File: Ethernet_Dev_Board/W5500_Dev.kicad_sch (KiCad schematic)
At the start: 35 parts, among them Q201 PMV48XPA2R, U201 WIZNET_W5500, U202 74AUP1T08GWH, Y201 25MHz

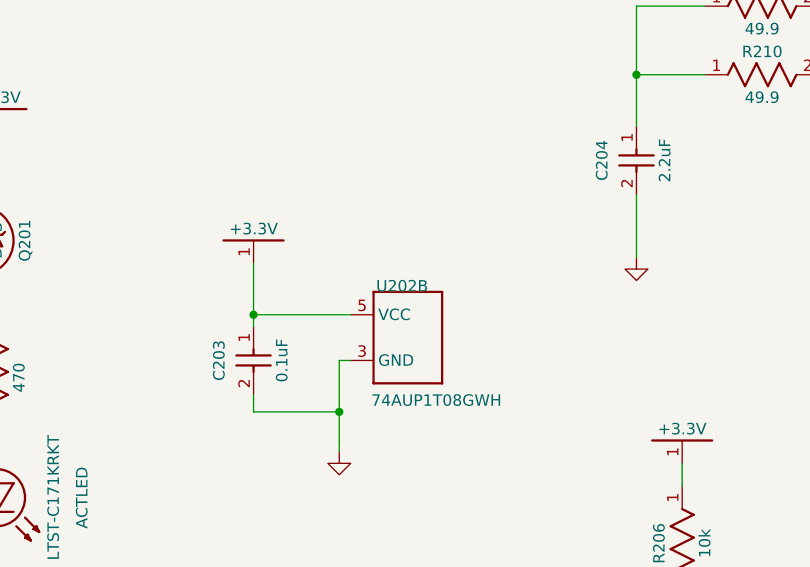
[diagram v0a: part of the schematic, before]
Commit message: Associating footprint to component
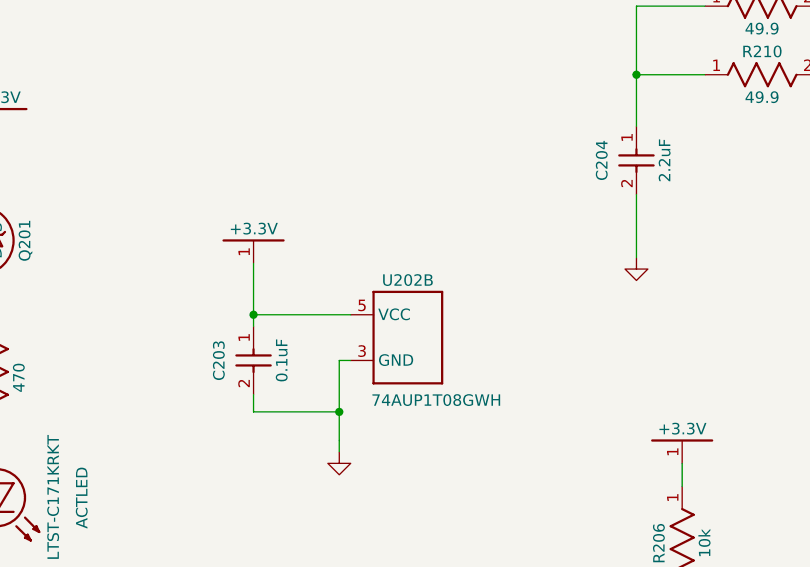
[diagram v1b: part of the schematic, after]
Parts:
- Y201: footprint (none) -> RG_Crystal:Crystal_SMD_4Pin_7.0mmx5.0mm
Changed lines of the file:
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@@
 			)
 		)
-		(property "Footprint" ""
+		(property "Footprint" "RG_Crystal:Crystal_SMD_4Pin_7.0mmx5.0mm"
 			(at 179.07 154.94 0)
 			(effects
@@
 		(dnp no)
 		(property "Reference" "U202"
-			(at 139.065 108.585 0)
-			(effects
-				(font
+			(at 139.7 107.95 0)
+			(effects
+				(font

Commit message: Net adjustments. Beginning board layout
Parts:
- LED201: value ACTLED -> 5500 ACT
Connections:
- net GNDS: no longer C201.2, C202.2, C203.2, C204.2, C205.2, C206.2, C209.2, C210.2, R201.2, R202.10 (1@2), R204.1, U201.14 (AGND@1), U201.16 (AGND@2), U201.19 (AGND@3), U201.29 (GND), U201.3 (AGND@1), U201.48 (AGND), U201.9 (AGND@2), U202.3 (GND), Y201.2 (GND)
- net RXN renamed RX_N
- net RXN_ETH renamed ETH_RX_N
- net RXP renamed RX_P
- net RXP_ETH renamed ETH_RX_P
- net TXN renamed TX_N
- net TXN_ETH renamed ETH_TX_N
- net TXP renamed TX_P
- net TXP_ETH renamed ETH_TX_P
- new net GND1: C201.2, C202.2, C203.2, C204.2, C205.2, C206.2, C209.2, C210.2, R201.2, R202.10 (1@2), R204.1, U201.14 (AGND@1), U201.16 (AGND@2), U201.19 (AGND@3), U201.29 (GND), U201.3 (AGND@1), U201.48 (AGND), U201.9 (AGND@2), U202.3 (GND), Y201.2 (GND)
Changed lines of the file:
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@@
 	(wire
 		(pts
-			(xy 53.975 65.405) (xy 53.975 86.995)
-		)
-		(stroke
-			(width 0.25)
-			(type solid)
-		)
-	)
-	(wire
-		(pts
 			(xy 125.095 196.85) (xy 41.275 196.85)
 		)
@@
 		)
 		(stroke
-			(width 0.25)
-			(type solid)
+			(width 0)
+			(type default)
 		)
 	)
@@
 		)
 		(stroke
-			(width 0.25)
-			(type solid)
+			(width 0)
+			(type default)
 		)
 	)
@@
 		)
 		(stroke
-			(width 0.25)
-			(type solid)
+			(width 0)
+			(type default)
 		)
 	)
@@
 		)
 		(stroke
-			(width 0.25)
-			(type solid)
+			(width 0)
+			(type default)
 		)
 	)
@@
 		)
 		(stroke
-			(width 0.25)
-			(type solid)
+			(width 0)
+			(type default)
 		)
 	)
@@
 		)
 		(stroke
-			(width 0.25)
-			(type solid)
+			(width 0)
+			(type default)
 		)
 	)
@@
 		)
 		(stroke
-			(width 0.25)
-			(type solid)
+			(width 0)
+			(type default)
 		)
 	)
@@
 		)
 		(stroke
-			(width 0.25)
-			(type solid)
+			(width 0)
+			(type default)
 		)
 	)
@@
 		)
 		(stroke
-			(width 0.25)
-			(type solid)
+			(width 0)
+			(type default)
 		)
 	)
@@
 		)
 		(stroke
-			(width 0.25)
-			(type solid)
+			(width 0)
+			(type default)
 		)
 	)
@@
 		)
 		(stroke
-			(width 0.25)
-			(type solid)
+			(width 0)
+			(type default)
 		)
 	)
@@
 	(wire
 		(pts
-			(xy 132.08 125.73) (xy 132.08 127)
+			(xy 132.08 122.555) (xy 132.08 127)
 		)
 		(stroke
@@
 	(wire
 		(pts
-			(xy 76.835 184.15) (xy 76.835 186.055)
+			(xy 76.835 182.88) (xy 76.835 186.055)
 		)
 		(stroke
@@
 		)
 		(stroke
-			(width 0.25)
-			(type solid)
+			(width 0)
+			(type default)
 		)
 	)
@@
 	(wire
 		(pts
-			(xy 34.925 173.99) (xy 34.925 177.165)
+			(xy 34.925 173.99) (xy 34.925 178.435)
 		)
 		(stroke
-			(width 0.25)
-			(type solid)
+			(width 0)
+			(type default)
 		)
 	)
@@
 	(wire
 		(pts
-			(xy 213.36 121.92) (xy 213.36 123.825)
+			(xy 213.36 118.11) (xy 213.36 123.825)
 		)
 		(stroke
@@
 	(wire
 		(pts
-			(xy 64.135 86.995) (xy 64.135 88.9)
+			(xy 64.135 85.725) (xy 64.135 88.9)
 		)
 		(stroke
@@
 		)
 		(stroke
-			(width 0.25)
-			(type solid)
+			(width 0)
+			(type default)
 		)
 	)
@@
 	(wire
 		(pts
-			(xy 34.925 177.165) (xy 34.925 178.435)
-		)
-		(stroke
-			(width 0)
-			(type default)
-		)
-	)
-	(wire
-		(pts
 			(xy 29.845 73.025) (xy 79.375 73.025)
 		)
@@
 		)
 		(stroke
-			(width 0.25)
-			(type solid)
+			(width 0)
+			(type default)
 		)
 	)
@@
 	(wire
 		(pts
-			(xy 213.36 118.11) (xy 213.36 121.92)
-		)
-		(stroke
-			(width 0.25)
-			(type solid)
-		)
-	)
-	(wire
-		(pts
 			(xy 121.285 191.77) (xy 46.355 191.77)
 		)
@@
 	(wire
 		(pts
-			(xy 53.975 86.995) (xy 53.975 88.9)
+			(xy 53.975 65.405) (xy 53.975 88.9)
 		)
 		(stroke
@@
 	(wire
 		(pts
-			(xy 132.08 125.73) (xy 132.08 122.555)
-		)
-		(stroke
-			(width 0.25)
-			(type solid)
-		)
-	)
-	(wire
-		(pts
 			(xy 29.845 70.485) (xy 43.815 70.485)
 		)
@@
 	(wire
 		(pts
-			(xy 76.835 182.88) (xy 76.835 184.15)
-		)
-		(stroke
-			(width 0.25)
-			(type solid)
-		)
-	)
-	(wire
-		(pts
 			(xy 234.95 52.07) (xy 262.89 52.07)
 		)
@@
 		)
 	)
-	(wire
-		(pts
-			(xy 64.135 85.725) (xy 64.135 86.995)
-		)
-		(stroke
-			(width 0.25)
-			(type solid)
-		)
-	)
 	(symbol
 		(lib_id "RG_resistors:RES-0603")
@@
 			)
 		)
-		(property "Value" "GNDS"
+		(property "Value" "GND1"
 			(at 132.08 132.08 0)
 			(effects
@@
 			)
 		)
-		(property "Value" "GNDS"
+		(property "Value" "GND1"
 			(at 170.18 161.29 0)
 			(effects
@@
 			)
 		)
-		(property "Value" "GNDS"
+		(property "Value" "GND1"
 			(at 53.346 135.261 0)
 			(effects
@@
 			)
 		)
-		(property "Value" "GNDS"
+		(property "Value" "GND1"
 			(at 190.5 165.1 0)
 			(effects
@@
 			)
 		)
-		(property "Value" "RXP_ETH"
+		(property "Value" "ETH_RX_P"
 			(at 270.51 39.37 0)
 			(effects
@@
 			)
 		)
-		(property "Value" "TXN"
+		(property "Value" "TX_N"
 			(at 180.975 55.88 0)
 			(effects
@@
 			)
 		)
-		(property "Value" "GNDS"
+		(property "Value" "GND1"
 			(at 34.925 183.515 0)
 			(effects
@@
 			)
 		)
-		(property "Value" "RXP"
+		(property "Value" "RX_P"
 			(at 117.475 38.735 0)
 			(effects
@@
 			)
 		)
-		(property "Value" "GNDS"
+		(property "Value" "GND1"
 			(at 276.86 154.94 0)
 			(effects
@@
 			)
 		)
-		(property "Value" "GNDS"
+		(property "Value" "GND1"
 			(at 53.975 93.98 0)
 			(effects
@@
 			)
 		)
-		(property "Value" "ACTLED"
+		(property "Value" "5500 ACT"
 			(at 103.511 132.086 0)
 			(effects
@@
 			)
 		)
-		(property "Value" "RXP"
+		(property "Value" "RX_P"
 			(at 180.34 39.37 0)
 			(effects
@@
 			)
 		)
-		(property "Value" "GNDS"
+		(property "Value" "GND1"
 			(at 165.1 110.49 0)
 			(effects
@@
 			)
 		)
-		(property "Value" "TXN"
+		(property "Value" "TX_N"
 			(at 116.84 26.035 0)
 			(effects
@@
 			)
 		)
-		(property "Value" "TXP"
+		(property "Value" "TX_P"
 			(at 116.84 28.575 0)
 			(effects
@@
 			)
 		)
-		(property "Value" "TXN_ETH"
+		(property "Value" "ETH_TX_N"
 			(at 270.51 55.88 0)
 			(effects
@@
 			)
 		)
-		(property "Value" "TXP_ETH"
+		(property "Value" "ETH_TX_P"
 			(at 270.51 52.07 0)
 			(effects
@@
 			)
 		)
-		(property "Value" "TXP"
+		(property "Value" "TX_P"
 			(at 180.975 52.07 0)
 			(effects
@@
 			)
 		)
-		(property "Value" "GNDS"
+		(property "Value" "GND1"
 			(at 106.68 62.23 0)
 			(effects
@@
 			)
 		)
-		(property "Value" "RXN_ETH"
+		(property "Value" "ETH_RX_N"
 			(at 270.51 45.72 0)
 			(effects
@@
 			)
 		)
-		(property "Value" "GNDS"
+		(property "Value" "GND1"
 			(at 64.135 93.98 0)
 			(effects
@@
 			)
 		)
-		(property "Value" "RXN"
+		(property "Value" "RX_N"
 			(at 117.475 36.195 0)
 			(effects
@@
 			)
 		)
-		(property "Value" "GNDS"
+		(property "Value" "GND1"
 			(at 116.205 76.835 0)
 			(effects
@@
 			)
 		)
-		(property "Value" "RXN"
+		(property "Value" "RX_N"
 			(at 180.34 45.72 0)
 			(effects
@@
 			)
 		)
-		(property "Value" "GNDS"
+		(property "Value" "GND1"
 			(at 76.835 191.135 0)
 			(effects
@@
 			)
 		)
-		(property "Value" "GNDS"
+		(property "Value" "GND1"
 			(at 213.36 128.905 0)
 			(effects

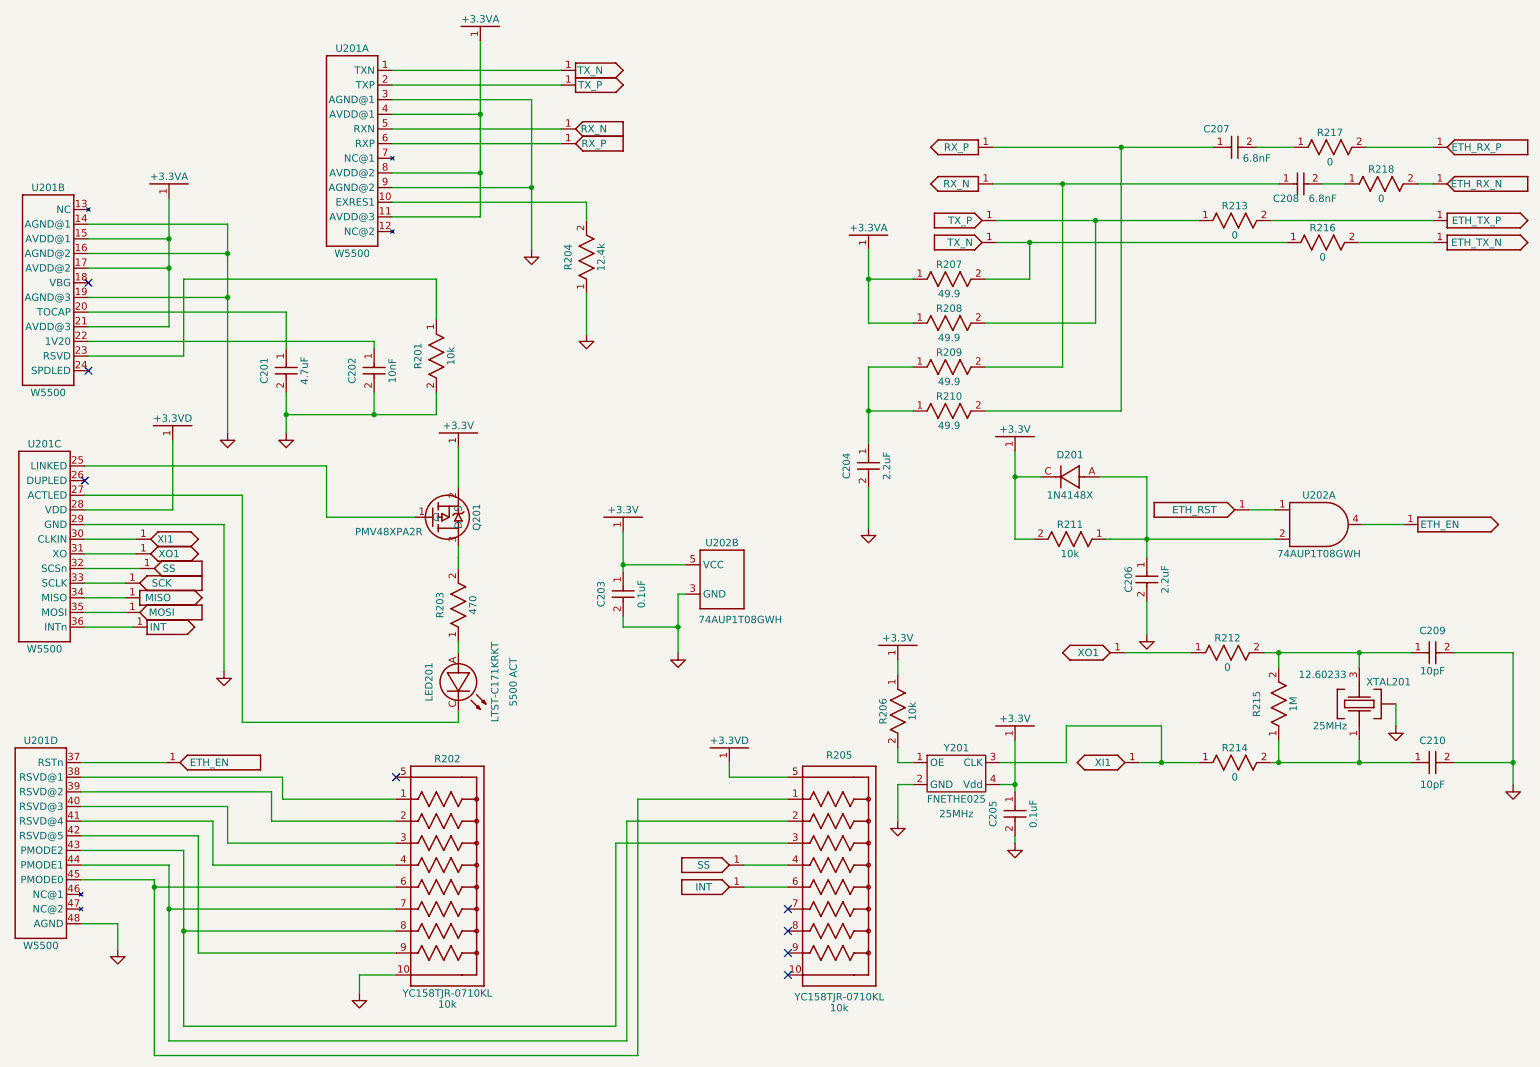
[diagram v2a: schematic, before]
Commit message: Removed 1 TVS diode. removed 1 reset circuit. Placed Ethernet port in both W5500 and W5100S circuits
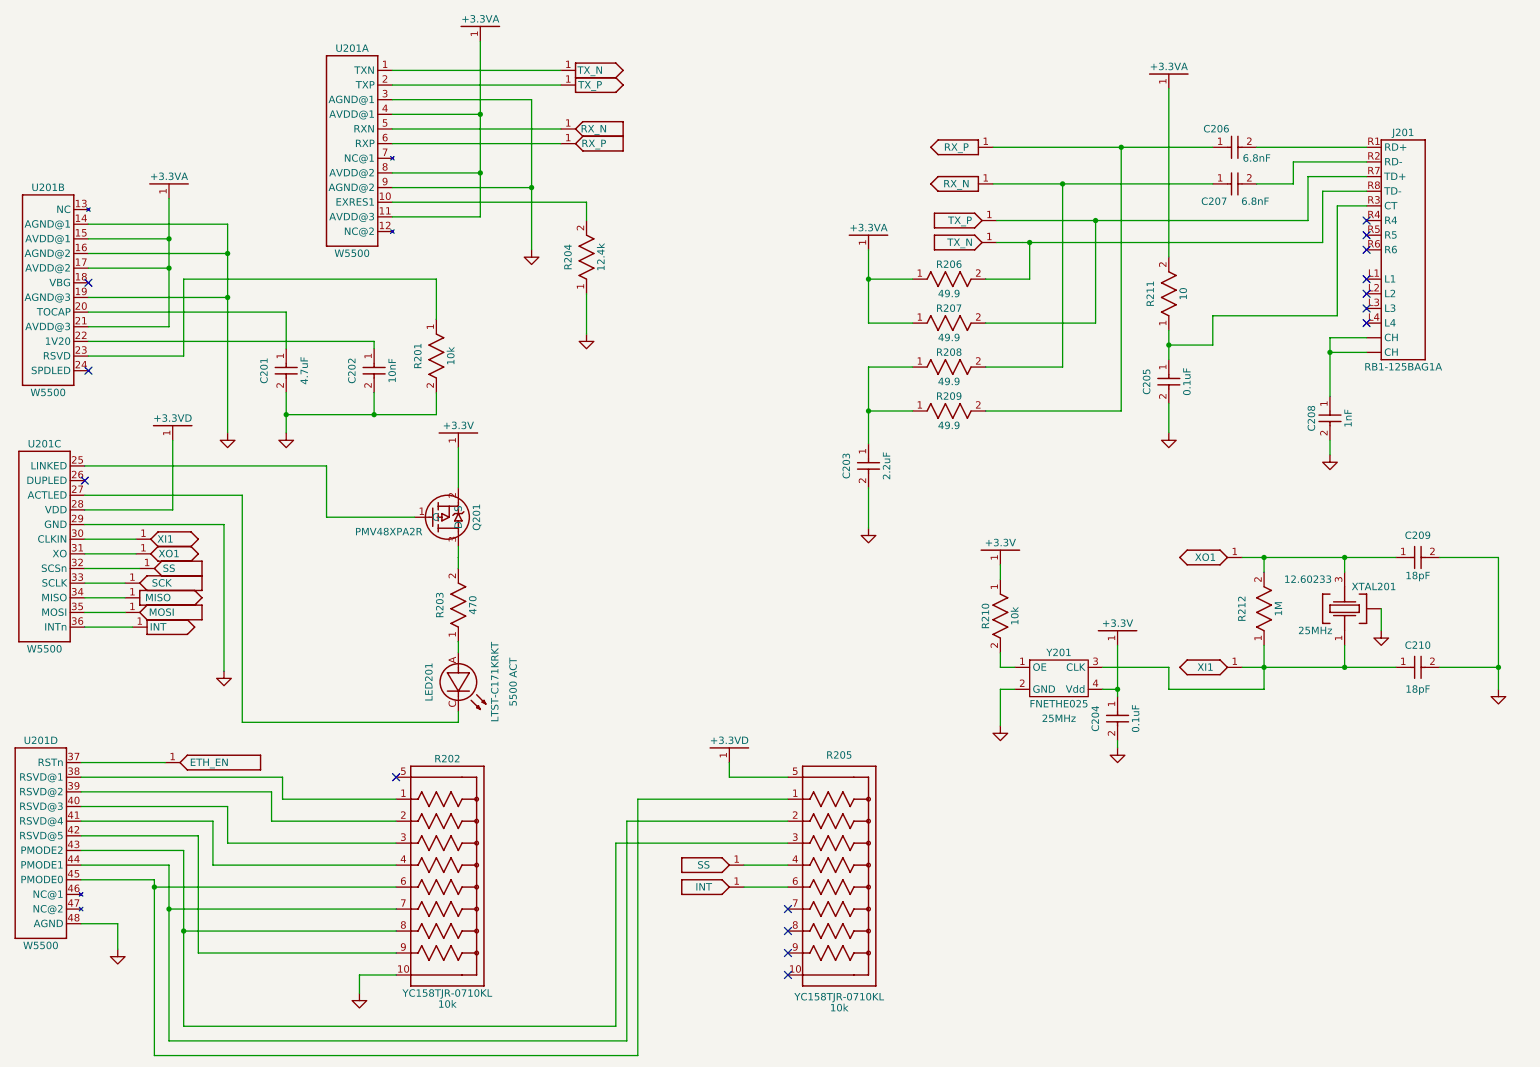
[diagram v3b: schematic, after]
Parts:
- removed C203: 0.1uF, RG_Capacitors_SMD:0603, symbol LED_Controller_Hardware-eagle-import:CAP-0603
- removed C206: 2.2uF, RG_Capacitors_SMD:0603, symbol LED_Controller_Hardware-eagle-import:CAP-0603
- removed D201: 1N4148X, RG_Diode:SOD-523-D, symbol LED_Controller_Hardware-eagle-import:1N4148X
- removed R212, R213, R214, R216, R217, R218: 0, RG_Resistors_SMD:0603, symbol RG_resistors:RES-0603
- removed U202: 74AUP1T08GWH, RG_TO_SOT_SMD:SOT23-5P65, symbol LED_Controller_Hardware-eagle-import:74AUP1T08GWH
- added C205: 0.1uF, RG_Capacitors_SMD:0603, symbol LED_Controller_Hardware-eagle-import:CAP-0603
- added C208: 1nF, RG_Capacitors_SMD:1206, symbol LED_Controller_Hardware-eagle-import:CAP-1206
- added J201: ~, RG_Connectors:WIZNET_RB1-125BAG1A, symbol RG_Connectors:RB1-125BAG1A
- C209, C210: value 10pF -> 18pF; Distributor PN 1276-1069-2-ND -> 738-CML0603C0G180JT50VTR-ND; Mfg. Samsung Electro-Mechanics -> Stackpole Electronics Inc; Mfg. PN CL10C100CB8NNNC -> CML0603C0G180JT50V
- R211: value 10k -> 10; Distributor PN RMCF0603FT10K0TR-ND -> RMCF0603FT10R0TR-ND; Mfg. PN RMCF0603FT10K0 -> RMCF0603FT10R0
- renumbered C204 to C203, C205 to C204, C207 to C206, C208 to C207, R207 to R206, R208 to R207, R209 to R208, R210 to R209, R206 to R210, R215 to R212
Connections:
- net +3.3V: no longer R211.2
- net +3.3VA: now also R211.2
- net GND1: now also C205.2, C208.2
- net TX_N: now also J201.R8 (TD-)
- net TX_P: now also J201.R7 (TD+)
- net XI1: now also C210.1, R212.1, XTAL201.1
- net XO1: now also C209.1, R212.2, XTAL201.3 (3@1)
- net at C206.2: now also J201.R1 (RD+)
- net at C207.2: now also J201.R2 (RD-)
- net at R211.1: now also C205.1, J201.R3 (CT)
- new net: C208.1, J201.S1 (CH), J201.S2 (CH)
- no-connect marks 8 -> 15
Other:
- moved on the sheet: C204, C207, C209, C210, R210, R212, XTAL201, Y201

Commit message: Removed unnecessary nets. Beginning board routing
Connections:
- net GNDS is gone; now on net GND1: XTAL201.2 (3@2)
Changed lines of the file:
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@@
 			)
 		)
-		(property "Value" "GNDS"
+		(property "Value" "GND1"
 			(at 254 128.27 0)
 			(effects

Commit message: Finished first version of routing the board. Also adjusted some nets
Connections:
- net RD+: now reaches C206.2, J201.R1 (RD+)
- net RD-: now reaches C207.2, J201.R2 (RD-)
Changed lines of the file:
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@@
+		)
+	)
+	(label "RD-"
+		(at 240.03 41.91 0)
+		(fields_autoplaced yes)
+		(effects
+			(font
+				(size 1.27 1.27)
+			)
+			(justify left bottom)
+		)
+	)
+	(label "RD+"
+		(at 240.03 39.37 0)
+		(fields_autoplaced yes)
+		(effects
+			(font
+				(size 1.27 1.27)
+			)
+			(justify left bottom)
 		)
 	)

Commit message: Updated part(s) due to out of stock
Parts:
- C208: Distributor PN 399-C1206C102KGRAC7800TR-ND -> 478-KGM31AR73D102MUTR-ND; Mfg. KEMET -> KYOCERA AVX; Mfg. PN C1206C102KGRAC7800 -> KGM31AR73D102MU
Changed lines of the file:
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@@
 			)
 		)
-		(property "Datasheet" "https://connect.kemet.com:7667/gateway/IntelliData-ComponentDocumentation/1.0/download/datasheet/C1206C102KGRACTU"
+		(property "Datasheet" "https://datasheets.kyocera-avx.com/HVKGM.pdf"
 			(at 245.11 86.36 0)
 			(effects
@@
 			)
 		)
-		(property "Mfg." "KEMET"
+		(property "Mfg." "KYOCERA AVX"
 			(at 245.11 86.36 0)
 			(effects
@@
 			)
 		)
-		(property "Mfg. PN" "C1206C102KGRAC7800"
+		(property "Mfg. PN" "KGM31AR73D102MU"
 			(at 245.11 86.36 0)
 			(effects
@@
 			)
 		)
-		(property "Distributor PN" "399-C1206C102KGRAC7800TR-ND"
+		(property "Distributor PN" "478-KGM31AR73D102MUTR-ND"
 			(at 245.11 86.36 0)
 			(effects
